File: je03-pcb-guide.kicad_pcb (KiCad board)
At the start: 2 copper layers, 69.8 x 38.1 mm, 24 parts, among them SW1 SW_Push, U1 ATmega32U4-AU, Y1 16MHz

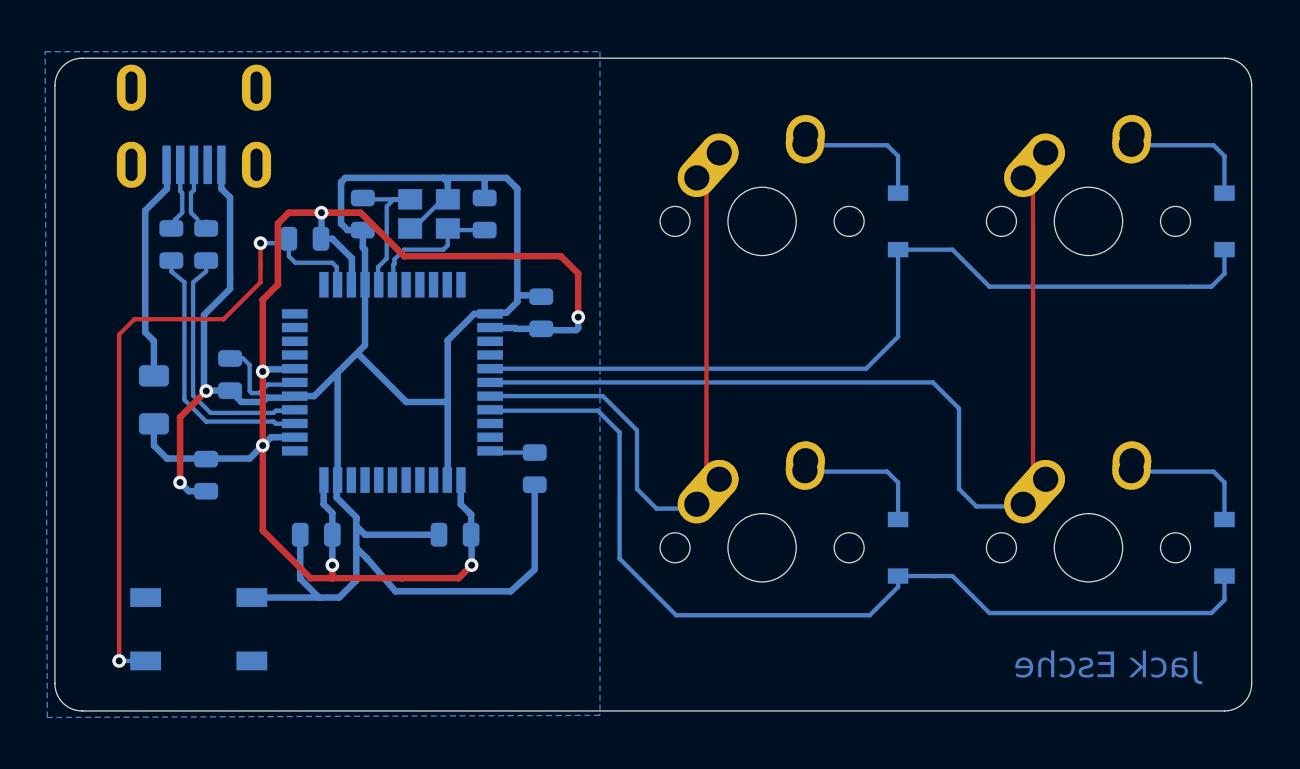
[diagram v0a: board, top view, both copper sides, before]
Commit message: Add USB-C
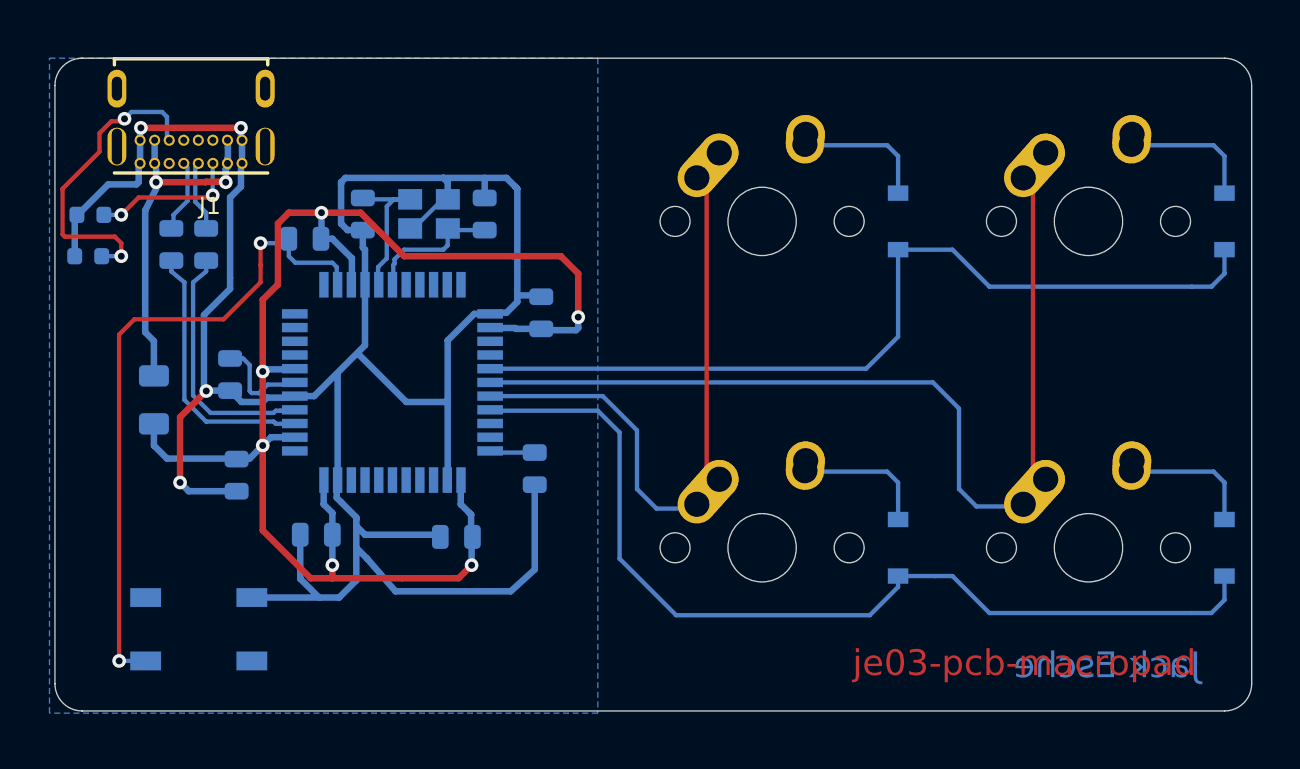
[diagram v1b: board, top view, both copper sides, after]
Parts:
- removed USB1: Molex-0548190589, random-keyboard-parts:Molex-0548190589
- added J1: USB4085-GF-A_REVA, USB4085-GF-A_REVA:GCT_USB4085-GF-A_REVA, F.Cu at (63.5, 81.5)
- added R5: 5.1k, Resistor_SMD:R_0603_1608Metric, B.Cu at (57.5, 90.9)
- added R6: 5.1k, Resistor_SMD:R_0603_1608Metric, B.Cu at (57.6, 88.5)
- moved C4 15.0 mm to (79.0, 107.3), turned to 180 degrees
- moved C7 13.2 mm to (66.2, 103.7), turned to 270 degrees
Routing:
- net GND: track 127.9 -> 146.3 mm, vias 2 -> 4
- net Net-(J1-PadB5): track 0.00 -> 18.1 mm, vias 0 -> 2
- net Net-(J1-PadA5): track 0.00 -> 8.35 mm, vias 0 -> 2
- net VCC: track 12.2 -> 19.7 mm, vias 0 -> 2
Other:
- board text added: "je03-pcb-macropad"

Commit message: USB-C
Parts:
- J1, MX1, MX2, MX3, MX4: moved to B.Cu
- moved D1 16.3 mm to (88.5, 89.0)
- moved D2 16.3 mm to (107.6, 89.0)
- moved D3 16.3 mm to (88.5, 108.0)
- moved D4 16.3 mm to (107.6, 108.0)
- turned J1 to 0 degrees
- turned MX1 to 180 degrees
- turned MX2 to 180 degrees
- turned MX3 to 180 degrees
- turned MX4 to 180 degrees
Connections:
- J1 pad P1: Net-(J1-PadP1) -> GND
- J1 pad P2: Net-(J1-PadP1) -> GND
- J1 pad P3: Net-(J1-PadP1) -> GND
- J1 pad P4: Net-(J1-PadP1) -> GND
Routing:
- net ROW1: track 55.7 -> 44.7 mm, vias 0 -> 2
- net COL0: track 32.9 -> 42.3 mm
- net COL1: track 53.5 -> 61.6 mm
- net ROW0: track 51.1 -> 44.5 mm
- net GND: track 146.3 -> 142.2 mm, vias 4 -> 2
- net Net-(J1-PadA5): track 8.35 -> 6.20 mm
- net Net-(J1-PadB5): track 18.1 -> 20.2 mm
- net D+: track 4.23 -> 6.04 mm, vias 0 -> 2
- net D-: track 4.03 -> 5.06 mm
- net Net-(D2-Pad2): track 6.74 -> 5.90 mm
- net Net-(D1-Pad2): track 6.74 -> 6.19 mm
- net VCC: track 19.7 -> 20.1 mm, vias 2 -> 0
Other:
- board text added: "Jack Esche August 2020"
- board text removed: "Jack Esche"

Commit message: Misc
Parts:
- moved F1 1.49 mm to (61.8, 97.9)
- moved C7 1.05 mm to (66.2, 102.7)
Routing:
- net Net-(C2-Pad1): track 8.29 -> 6.77 mm
- net GND: track 142.2 -> 141.0 mm
- net VCC: track 20.1 -> 19.2 mm
- net +5V: track 83.7 -> 83.0 mm
- added copper zone on F.Cu, net GND
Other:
- board text removed: "Jack Esche August 2020"

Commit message: Create Gerbers
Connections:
- J1 pad B6: Net-(J1-PadB6) -> D+
- J1 pad B7: Net-(J1-PadB7) -> D-
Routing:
- net D+: track 6.04 -> 7.82 mm
- net D-: track 5.06 -> 6.71 mm
